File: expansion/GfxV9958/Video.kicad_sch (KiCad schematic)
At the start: 39 parts, among them J3 S-Video, J4 Composite, J5 RGB Video, J6 Audio In, Q1 2N3904, U3 74HCT04, U4 CXA2075M, Y1 4.4336161875Mhz

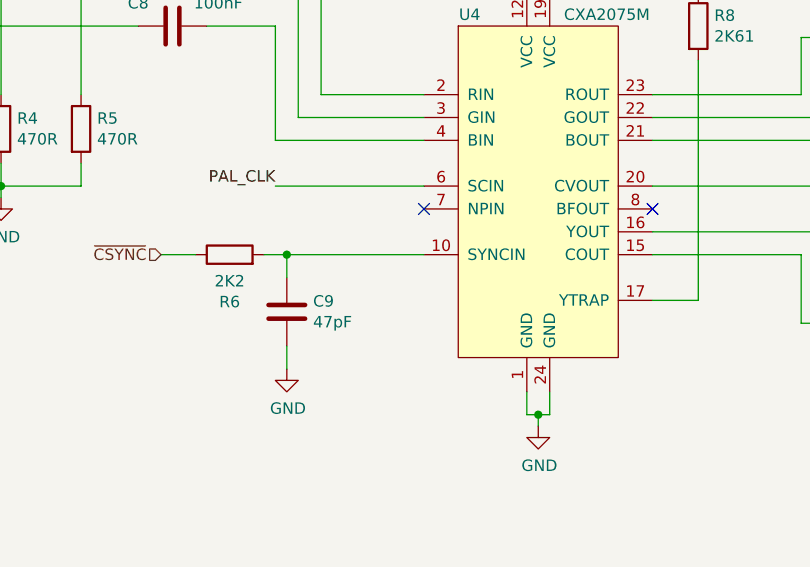
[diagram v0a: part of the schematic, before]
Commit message: Fix for CXA PAL issue and more
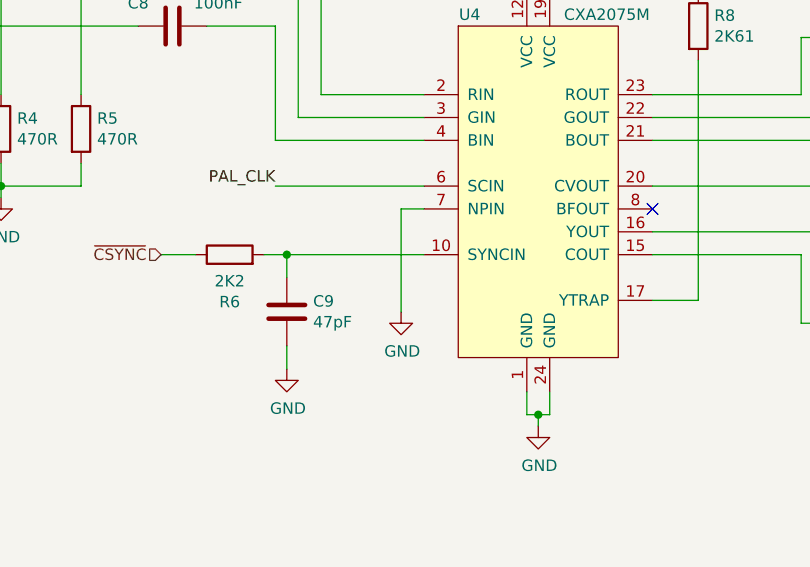
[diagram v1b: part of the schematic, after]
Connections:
- net GND: now also U4.7 (NPIN)
- no-connect marks 6 -> 5
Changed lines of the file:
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@@
   (no_connect (at 147.32 175.26))
   (no_connect (at 111.76 175.26))
-  (no_connect (at 100.33 59.69))
   (no_connect (at 125.73 59.69))
   (no_connect (at 111.76 162.56))
@@
     (stroke (width 0) (type default) (color 0 0 0 0))
   )
+  (wire (pts (xy 100.33 59.69) (xy 97.79 59.69))
+    (stroke (width 0) (type default) (color 0 0 0 0))
+  )
   (wire (pts (xy 62.23 57.15) (xy 53.34 57.15))
     (stroke (width 0) (type default) (color 0 0 0 0))
@@
   )
   (wire (pts (xy 193.04 46.99) (xy 182.88 46.99))
+    (stroke (width 0) (type default) (color 0 0 0 0))
+  )
+  (wire (pts (xy 97.79 59.69) (xy 97.79 71.12))
     (stroke (width 0) (type default) (color 0 0 0 0))
   )
@@
     (pin "1")
     (pin "2")
+    (pin "3")
+    (pin "4")
+    (pin "5")
+    (pin "6")
+    (pin "8")
+    (pin "9")
+    (pin "10")
+    (pin "11")
+    (pin "12")
+    (pin "13")
+    (pin "14")
+    (pin "7")
   )
   (symbol (lib_id "74xx:74HCT04") (at 93.98 118.11 0) (unit 2)
@@
       (effects (font (size 1.27 1.27)) hide)
     )
+    (pin "1")
+    (pin "2")
     (pin "3")
     (pin "4")
+    (pin "5")
+    (pin "6")
+    (pin "8")
+    (pin "9")
+    (pin "10")
+    (pin "11")
+    (pin "12")
+    (pin "13")
+    (pin "14")
+    (pin "7")
   )
   (symbol (lib_id "74xx:74HCT04") (at 119.38 175.26 0) (mirror y) (unit 3)
@@
       (effects (font (size 1.27 1.27)) hide)
     )
+    (pin "1")
+    (pin "2")
+    (pin "3")
+    (pin "4")
     (pin "5")
     (pin "6")
+    (pin "8")
+    (pin "9")
+    (pin "10")
+    (pin "11")
+    (pin "12")
+    (pin "13")
+    (pin "14")
+    (pin "7")
   )
   (symbol (lib_id "74xx:74HCT04") (at 119.38 162.56 0) (mirror y) (unit 4)
@@
       (effects (font (size 1.27 1.27)) hide)
     )
+    (pin "1")
+    (pin "2")
+    (pin "3")
+    (pin "4")
+    (pin "5")
+    (pin "6")
     (pin "8")
     (pin "9")
+    (pin "10")
+    (pin "11")
+    (pin "12")
+    (pin "13")
+    (pin "14")
+    (pin "7")
   )
   (symbol (lib_id "74xx:74HCT04") (at 139.7 162.56 0) (unit 5)
@@
       (effects (font (size 1.27 1.27)) hide)
     )
+    (pin "1")
+    (pin "2")
+    (pin "3")
+    (pin "4")
+    (pin "5")
+    (pin "6")
+    (pin "8")
+    (pin "9")
     (pin "10")
     (pin "11")
+    (pin "12")
+    (pin "13")
+    (pin "14")
+    (pin "7")
   )
   (symbol (lib_id "74xx:74HCT04") (at 139.7 175.26 0) (unit 6)
@@
       (effects (font (size 1.27 1.27)) hide)
     )
+    (pin "1")
+    (pin "2")
+    (pin "3")
+    (pin "4")
+    (pin "5")
+    (pin "6")
+    (pin "8")
+    (pin "9")
+    (pin "10")
+    (pin "11")
     (pin "12")
     (pin "13")
+    (pin "14")
+    (pin "7")
   )
   (symbol (lib_id "74xx:74HCT04") (at 43.18 171.45 0) (unit 7)
@@
       (effects (font (size 1.27 1.27)) hide)
     )
+    (pin "1")
+    (pin "2")
+    (pin "3")
+    (pin "4")
+    (pin "5")
+    (pin "6")
+    (pin "8")
+    (pin "9")
+    (pin "10")
+    (pin "11")
+    (pin "12")
+    (pin "13")
     (pin "14")
     (pin "7")
@@
       (effects (font (size 1.27 1.27)) hide)
     )
+    (pin "1")
+  )
+  (symbol (lib_id "power:GND") (at 97.79 71.12 0) (unit 1)
+    (in_bom yes) (on_board yes)
+    (property "Reference" "#PWR?" (id 0) (at 97.79 77.47 0)
+      (effects (font (size 1.27 1.27)) hide)
+    )
+    (property "Value" "GND" (id 1) (at 97.917 75.5142 0))
+    (property "Footprint" "" (id 2) (at 97.79 71.12 0)
+      (effects (font (size 1.27 1.27)) hide)
+    )
+    (property "Datasheet" "" (id 3) (at 97.79 71.12 0)
+      (effects (font (size 1.27 1.27)) hide)
+    )
